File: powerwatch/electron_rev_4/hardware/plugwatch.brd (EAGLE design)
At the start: 57.1 x 93 mm, 117 parts, among them J1 DM3AT-SF-PEJM5, J2 TC2030-JLINK-NL, U1 BGA725L6-ALT, U10 SIP32510, U11 SIP32510, U12 SIP32510, U13 SIP32510, U14 MPU-9250, U2 SAFFB1G56KB0F0A, U3 ISL29035, U4 MAX-M8, U5 MAX740XESA, U6 SIP32510, U7 NRF51822QF, U8 OPA322AIDBVT, U9 SIP32510, X1 32.768k, X2 16MHz

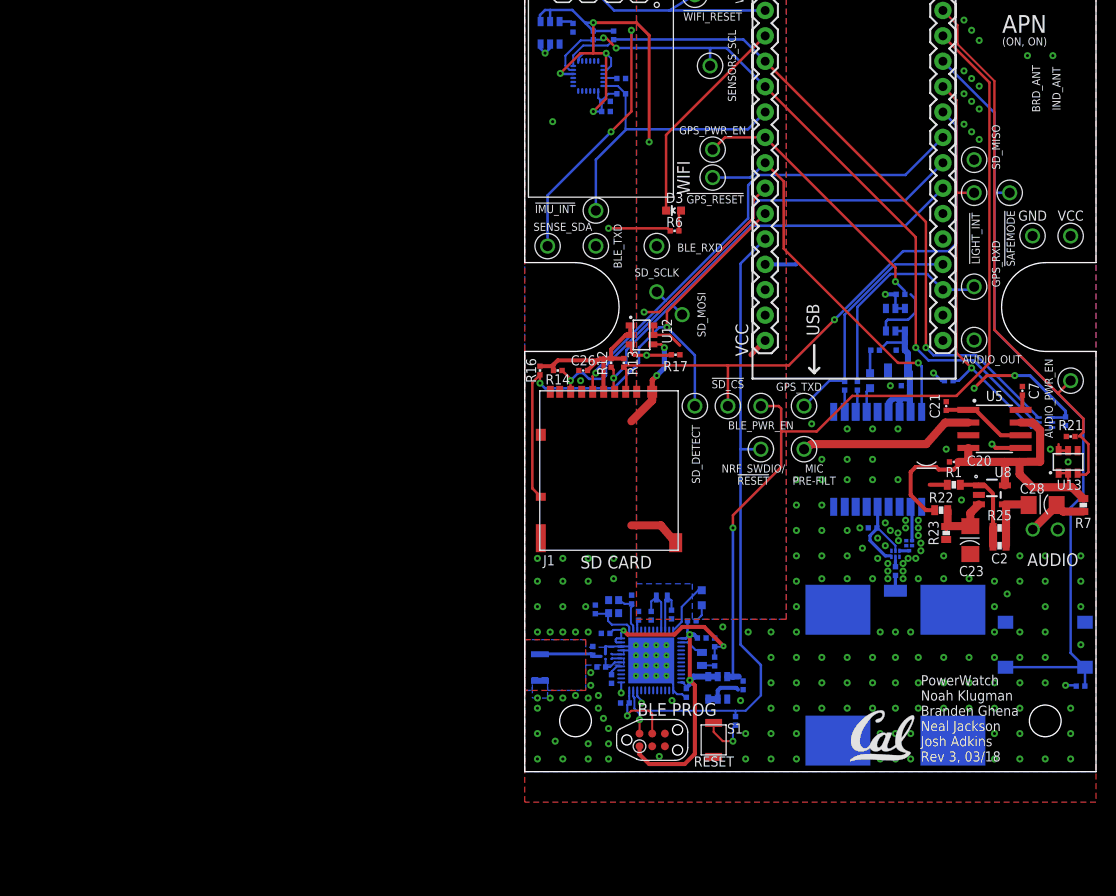
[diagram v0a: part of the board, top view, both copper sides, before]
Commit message: added power supervisory circuit
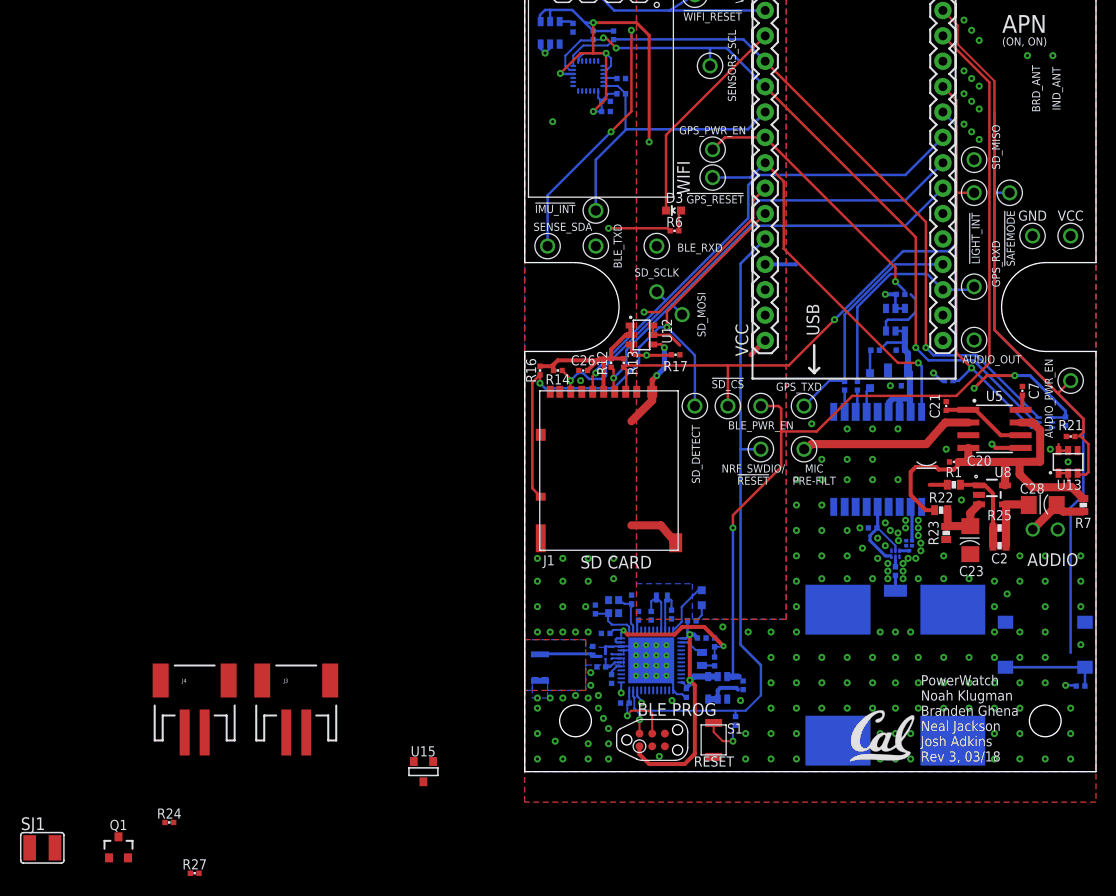
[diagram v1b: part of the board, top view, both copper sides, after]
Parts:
- added J3, J4: (no value), SparkFun-Connectors:JST-2-SMD
- added Q1: SI223DDS, fets:SOT23-3
- added R24: 10.4k, passives:0402_RES
- added R27: 101k, passives:0402_RES
- added SJ1: (no value), jumper:SJW
- added U15: TPS3839G25DBZ, chips:SOT-23
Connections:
- new net !EXTERNAL_RST: ASSY1.RST, Q1.1, U15.2
- new net !SOFT_RST: ASSY1.A0, R3.2, S2.3, S2.4
- new net N$23: J3.2, Q1.2, R24.1, SJ1.1
- new net N$30: R24.2, R27.1, U15.3
- new net N$35: J4.2, Q1.3, SJ1.2
- net !SAFEMODE: no longer ASSY1.A0, R3.2, S2.3, S2.4
- net GND: now also J3.1, J4.1, R27.2, U15.1
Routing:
- net !SAFEMODE: track 78.9 -> 59.8 mm
- net !SOFT_RST: track 0.00 -> 9.84 mm
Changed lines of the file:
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@@
 <attribute name="VALUE" x="43.053" y="88.9" size="1.016" layer="28" font="vector" ratio="12" rot="MR270" align="bottom-center"/>
 </element>
+<element name="U15" library="chips" package="SOT-23" value="TPS3839G25DBZ" x="-10.16" y="0">
+<attribute name="DIGIKEY" value="296-42522-1-ND" x="-10.16" y="0" size="1.778" layer="27" font="vector" ratio="12" display="off"/>
+<attribute name="MANUFACTURER" value="TEXAS INSTRUMENTS" x="-10.16" y="0" size="1.778" layer="27" font="vector" ratio="12" display="off"/>
+<attribute name="MPN" value="TPS3839G25DBZR" x="-10.16" y="0" size="1.778" layer="27" font="vector" ratio="12" display="off"/>
+</element>
+<element name="J3" library="SparkFun-Connectors" package="JST-2-SMD" value="" x="-22.86" y="7.62">
+<attribute name="PROD_ID" value="CONN-08352" x="-22.86" y="7.62" size="1.778" layer="27" font="vector" ratio="12" display="off"/>
+</element>
+<element name="J4" library="SparkFun-Connectors" package="JST-2-SMD" value="" x="-33.02" y="7.62">
+<attribute name="PROD_ID" value="CONN-08352" x="-33.02" y="7.62" size="1.778" layer="27" font="vector" ratio="12" display="off"/>
+</element>
+<element name="R24" library="passives" package="0402_RES" value="10.4k" x="-35.56" y="-5.08">
+<attribute name="DESCRIPTION" value="RES SMD 150 OHM 1% 1/16W 0402" x="-33.02" y="-5.08" size="1.778" layer="27" font="vector" ratio="12" display="off"/>
+<attribute name="DIGIKEY" value="RMCF0402FT150RCT-ND" x="-33.02" y="-5.08" size="1.778" layer="27" font="vector" ratio="12" display="off"/>
+<attribute name="MANUFACTURER" value="Stackpole Electronics" x="-33.02" y="-5.08" size="1.778" layer="27" font="vector" ratio="12" display="off"/>
+<attribute name="MPN" value="RMCF0402FT150R" x="-33.02" y="-5.08" size="1.778" layer="27" font="vector" ratio="12" display="off"/>
+</element>
+<element name="R27" library="passives" package="0402_RES" value="101k" x="-33.02" y="-10.16">
+<attribute name="DESCRIPTION" value="RES SMD 150 OHM 1% 1/16W 0402" x="-33.02" y="-10.16" size="1.778" layer="27" font="vector" ratio="12" display="off"/>
+<attribute name="DIGIKEY" value="RMCF0402FT150RCT-ND" x="-33.02" y="-10.16" size="1.778" layer="27" font="vector" ratio="12" display="off"/>
+<attribute name="MANUFACTURER" value="Stackpole Electronics" x="-33.02" y="-10.16" size="1.778" layer="27" font="vector" ratio="12" display="off"/>
+<attribute name="MPN" value="RMCF0402FT150R" x="-33.02" y="-10.16" size="1.778" layer="27" font="vector" ratio="12" display="off"/>
+</element>
+<element name="Q1" library="fets" package="SOT23-3" value="SI223DDS" x="-40.64" y="-7.62">
+<attribute name="DIGIKEY" value="SI2333DDS-T1-GE3CT-ND" x="-40.64" y="-7.62" size="1.778" layer="27" font="vector" ratio="12" display="off"/>
+<attribute name="MANUFACTURER" value="Vishay Siliconix" x="-40.64" y="-7.62" size="1.778" layer="27" font="vector" ratio="12" display="off"/>
+<attribute name="MPN" value="SI2333DDS-T1-GE3" x="-40.64" y="-7.62" size="1.778" layer="27" font="vector" ratio="12" display="off"/>
+</element>
+<element name="SJ1" library="jumper" library_urn="urn:adsk.eagle:library:252" package="SJW" package3d_urn="urn:adsk.eagle:package:15507/1" value="" x="-48.26" y="-7.62"/>
 </elements>
 <signals>
@@
 </signal>
 <signal name="!SAFEMODE">
-<contactref element="ASSY1" pad="A0"/>
-<contactref element="R3" pad="2"/>
-<contactref element="S2" pad="3"/>
-<contactref element="S2" pad="4"/>
 <contactref element="TP8" pad="TESTPOINT"/>
 <wire x1="46.99" y1="44.196" x2="46.99" y2="57.912" width="0.254" layer="16"/>
 <wire x1="46.99" y1="57.912" x2="46.99" y2="65.913" width="0.254" layer="16"/>
-<wire x1="46.99" y1="65.913" x2="41.8338" y2="71.0692" width="0.254" layer="16"/>
-<wire x1="48.095" y1="10.45" x2="56.045" y2="10.45" width="0.254" layer="16"/>
 <wire x1="48.514" y1="57.912" x2="46.99" y2="57.912" width="0.254" layer="16"/>
 <wire x1="54.61" y1="11.885" x2="54.61" y2="26.416" width="0.254" layer="16"/>
@@
 <wire x1="55.88" y1="27.686" x2="55.88" y2="35.306" width="0.254" layer="16"/>
 <wire x1="55.88" y1="35.306" x2="46.99" y2="44.196" width="0.254" layer="16"/>
-<wire x1="56.03366875" y1="8.5598" x2="56.045" y2="8.57113125" width="0.254" layer="16"/>
-<wire x1="56.045" y1="10.45" x2="54.61" y2="11.885" width="0.254" layer="16"/>
-<wire x1="56.045" y1="8.57113125" x2="56.045" y2="10.45" width="0.254" layer="16"/>
 </signal>
 <signal name="!SD_CS">
@@
 <contactref element="R21" pad="1"/>
 <contactref element="R17" pad="1"/>
+<contactref element="J3" pad="1"/>
+<contactref element="U15" pad="1"/>
+<contactref element="R27" pad="2"/>
+<contactref element="J4" pad="1"/>
 <wire x1="50.292" y1="71.628" x2="52.832" y2="71.628" width="0" layer="19" extent="1-1"/>
 <wire x1="45.466" y1="73.152" x2="50.292" y2="71.628" width="0" layer="19" extent="1-1"/>
@@
 <wire x1="10.668" y1="35.052" x2="5.701" y2="38" width="0" layer="19" extent="1-1"/>
 <wire x1="14.65453125" y1="41.7068" x2="13.97" y2="42.418" width="0" layer="19" extent="1-1"/>
+<wire x1="-9.1694" y1="1.016" x2="1.27" y2="1.27" width="0" layer="19" extent="1-1"/>
+<wire x1="-23.86" y1="3.92" x2="-9.1694" y2="1.016" width="0" layer="19" extent="1-1"/>
+<wire x1="-34.02" y1="3.92" x2="-23.86" y2="3.92" width="0" layer="19" extent="1-1"/>
+<wire x1="-32.58693125" y1="-10.16" x2="-34.02" y2="3.92" width="0" layer="19" extent="1-1"/>
 <wire x1="32.004" y1="88.647" x2="43.942" y2="75.184" width="0" layer="19" extent="16-16"/>
 <wire x1="28.956" y1="89.916" x2="32.004" y2="88.647" width="0" layer="19" extent="16-16"/>
@@
 <wire x1="47.7012" y1="86.3092" x2="48.26" y2="86.868" width="0.1524" layer="1"/>
 </signal>
+<signal name="N$23">
+<contactref element="J3" pad="2"/>
+<contactref element="R24" pad="1"/>
+<contactref element="Q1" pad="2"/>
+<contactref element="SJ1" pad="1"/>
+<wire x1="-39.69" y1="-8.62" x2="-49.53" y2="-7.62" width="0" layer="19" extent="1-1"/>
+<wire x1="-35.99306875" y1="-5.08" x2="-39.69" y2="-8.62" width="0" layer="19" extent="1-1"/>
+<wire x1="-21.86" y1="3.92" x2="-35.99306875" y2="-5.08" width="0" layer="19" extent="1-1"/>
+</signal>
+<signal name="N$30">
+<contactref element="R24" pad="2"/>
+<contactref element="R27" pad="1"/>
+<contactref element="U15" pad="3"/>
+<wire x1="-35.12693125" y1="-5.08" x2="-33.45306875" y2="-10.16" width="0" layer="19" extent="1-1"/>
+<wire x1="-10.1346" y1="-1.016" x2="-33.45306875" y2="-10.16" width="0" layer="19" extent="1-1"/>
+</signal>
+<signal name="!EXTERNAL_RST">
+<contactref element="U15" pad="2"/>
+<contactref element="Q1" pad="1"/>
+<contactref element="ASSY1" pad="RST"/>
+<wire x1="-11.0998" y1="1.016" x2="24.0538" y2="45.6692" width="0" layer="19" extent="1-1"/>
+<wire x1="-41.59" y1="-8.62" x2="-11.0998" y2="1.016" width="0" layer="19" extent="1-1"/>
+</signal>
+<signal name="N$35">
+<contactref element="Q1" pad="3"/>
+<contactref element="J4" pad="2"/>
+<contactref element="SJ1" pad="2"/>
+<wire x1="-40.64" y1="-6.52" x2="-46.99" y2="-7.62" width="0" layer="19" extent="1-1"/>
+<wire x1="-32.02" y1="3.92" x2="-40.64" y2="-6.52" width="0" layer="19" extent="1-1"/>
+</signal>
+<signal name="!SOFT_RST">
+<contactref element="R3" pad="2"/>
+<contactref element="S2" pad="3"/>
+<contactref element="S2" pad="4"/>
+<wire x1="48.095" y1="10.45" x2="56.045" y2="10.45" width="0.254" layer="16"/>
+<wire x1="56.03366875" y1="8.5598" x2="56.045" y2="8.57113125" width="0.254" layer="16"/>
+<wire x1="56.045" y1="8.57113125" x2="56.045" y2="10.45" width="0.254" layer="16"/>
+<contactref element="ASSY1" pad="A0"/>
+<wire x1="48.095" y1="10.45" x2="41.8338" y2="71.0692" width="0" layer="19" extent="16-16"/>
+</signal>
 </signals>
 <errors>
@@
 with this version.
 </note>
+<note version="8.3" severity="warning">
+Since Version 8.3, EAGLE supports URNs for individual library
+assets (packages, symbols, and devices). The URNs of those assets
+will not be understood (or retained) with this version.
+</note>
+<note version="8.3" severity="warning">
+Since Version 8.3, EAGLE supports the association of 3D packages
+with devices in libraries, schematics, and board files. Those 3D
+packages will not be understood (or retained) with this version.
+</note>
 </compatibility>
